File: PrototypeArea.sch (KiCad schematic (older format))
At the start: 16 parts, among them P12 CONN_20, P14 CONN_20, P15 CONN_5, P16 CONN_20, P17 CONN_20, P18 CONN_20, P19 CONN_20, P20 CONN_20, P21 CONN_20, P22 CONN_20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

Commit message: Changed the footprint of the PIC to the correct one. Changed the layout of the development area, to be more suited for development Changed the layout of the reset button and programmer header. The programmer header now needs to be a 90deg header, for the pickit3 to fit Added components for the mounting holes and OSHW logos.
Signed-off-by: Kolijn Wolfaardt <kolijn.wolfaardt2gmail.com>
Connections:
- wire segments 58 -> 70

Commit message: Changed to FTDI chip, cut space from development area
An FTDI chip was added to provide the USB communications rather than the PIC
A jumper is available to choose if the USB datalines go to the FTDI chip or the
PIC.

The development area was reduced to provide space for the FTDI chip.

Signed-off-by: Kolijn Wolfaardt <kolijn.wolfaardt@gmail.com>
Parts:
- removed P12, P14, P16, P17, P18, P19, P20, P21, P22, P5, P6, P7: CONN_20, symbol CONN_20
- added P12, P14, P16, P17, P18, P19, P20, P21, P22, P5, P6, P7: CONN_12, symbol CONN_12
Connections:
- wire segments 70 -> 40

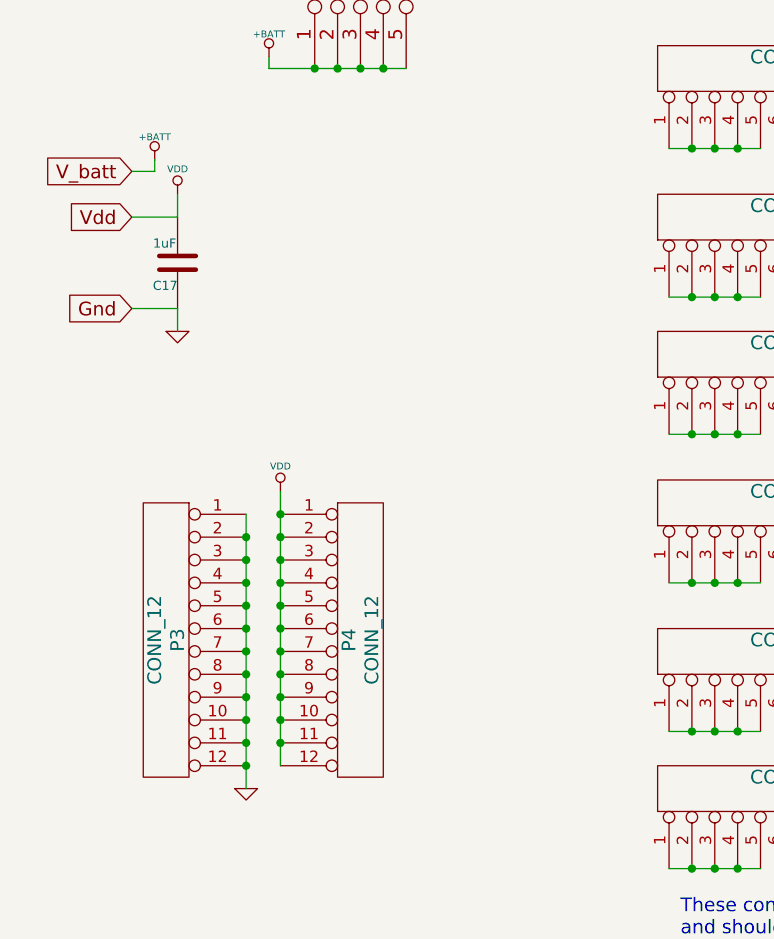
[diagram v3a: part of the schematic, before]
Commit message: Changed the board to use 3.3v rather than 5v. Total new layout.
Since the FTDI chip cannot communicate with the 5v PIC. So run
the PIC at 3.3v This limits the maximum crystal frequency of
the pic, but 4MHz is fine. the internal usb regulator is no
longer used and is replaced with the external one.

The 3.3v regulator get it's 5v from the selected 5v source.
5v is still used by the FTDI chip and the Motor driver.

Signed-off-by: Kolijn Wolfaardt <kolijn.wolfaardt@gmail.com>
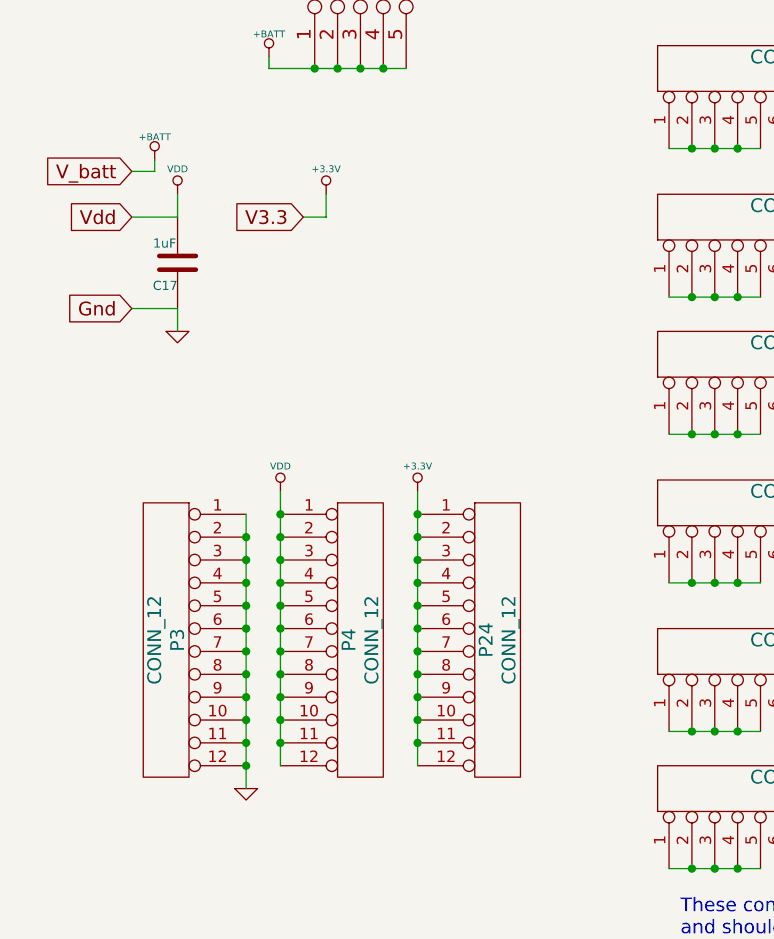
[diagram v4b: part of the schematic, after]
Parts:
- added P24: CONN_12, symbol CONN_12
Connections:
- new net +3.3V: P24.1 (P1), P24.10 (P10), P24.11 (P11), P24.12 (P12), P24.2 (P2), P24.3 (P3), P24.4 (P4), P24.5 (P5), P24.6 (P6), P24.7 (P7), P24.8 (P8), P24.9 (P9)
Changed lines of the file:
@@
 LIBS:l293
 LIBS:FT230x
+LIBS:33vReg
 LIBS:Robotics Board-cache
 EELAYER 27 0
@@
 Sheet 6 6
 Title ""
-Date "19 apr 2014"
+Date "20 apr 2014"
 Rev ""
 Comp ""
@@
 $EndDescr
 $Comp
-L +BATT #PWR054
+L +BATT #PWR061
 U 1 1 52F479E1
 P 1900 1100
-F 0 "#PWR054" H 1900 1050 20  0001 C CNN
+F 0 "#PWR061" H 1900 1050 20  0001 C CNN
 F 1 "+BATT" H 1900 1200 30  0000 C CNN
 F 2 "" H 1900 1100 60  0000 C CNN
@@
 $EndComp
 $Comp
-L GND #PWR055
+L GND #PWR062
 U 1 1 52F47A1B
 P 1800 4300
-F 0 "#PWR055" H 1800 4300 30  0001 C CNN
+F 0 "#PWR062" H 1800 4300 30  0001 C CNN
 F 1 "GND" H 1800 4230 30  0001 C CNN
 F 2 "" H 1800 4300 60  0000 C CNN
@@
 $EndComp
 $Comp
-L VDD #PWR056
+L VDD #PWR063
 U 1 1 52F47A2F
 P 1950 3000
-F 0 "#PWR056" H 1950 3100 30  0001 C CNN
+F 0 "#PWR063" H 1950 3100 30  0001 C CNN
 F 1 "VDD" H 1950 3110 30  0000 C CNN
 F 2 "" H 1950 3000 60  0000 C CNN
@@
 V_batt
 $Comp
-L +BATT #PWR057
+L +BATT #PWR064
 U 1 1 52F8A3F3
 P 1400 1550
-F 0 "#PWR057" H 1400 1500 20  0001 C CNN
+F 0 "#PWR064" H 1400 1500 20  0001 C CNN
 F 1 "+BATT" H 1400 1650 30  0000 C CNN
 F 2 "" H 1400 1550 60  0000 C CNN
@@
 $EndComp
 $Comp
-L GND #PWR058
+L GND #PWR065
 U 1 1 52F8A5C7
 P 1500 2300
-F 0 "#PWR058" H 1500 2300 30  0001 C CNN
+F 0 "#PWR065" H 1500 2300 30  0001 C CNN
 F 1 "GND" H 1500 2230 30  0001 C CNN
 F 2 "" H 1500 2300 60  0000 C CNN
@@
 $EndComp
 $Comp
-L VDD #PWR059
+L VDD #PWR066
 U 1 1 52F8A5CD
 P 1500 1700
-F 0 "#PWR059" H 1500 1800 30  0001 C CNN
+F 0 "#PWR066" H 1500 1800 30  0001 C CNN
 F 1 "VDD" H 1500 1810 30  0000 C CNN
 F 2 "" H 1500 1700 60  0000 C CNN
@@
 Connection ~ 5650 1600
 Connection ~ 6050 4650
+$Comp
+L CONN_12 P24
+U 1 1 53538B70
+P 2900 3650
+F 0 "P24" V 2850 3650 60  0000 C CNN
+F 1 "CONN_12" V 2950 3650 60  0000 C CNN
+F 2 "" H 2900 3650 60  0000 C CNN
+F 3 "" H 2900 3650 60  0000 C CNN
+	1    2900 3650
+	1    0    0    -1
+$EndComp
+Wire Wire Line
+	2550 3000 2550 4200
+Connection ~ 2550 4100
+Connection ~ 2550 4000
+Connection ~ 2550 3900
+Connection ~ 2550 3800
+Connection ~ 2550 3700
+Connection ~ 2550 3600
+Connection ~ 2550 3500
+Connection ~ 2550 3400
+Connection ~ 2550 3300
+Connection ~ 2550 3200
+Text GLabel 2050 1800 0    60   Input ~ 0
+V3.3
+$Comp
+L +3.3V #PWR067
+U 1 1 53539288
+P 2150 1700
+F 0 "#PWR067" H 2150 1660 30  0001 C CNN
+F 1 "+3.3V" H 2150 1810 30  0000 C CNN
+F 2 "" H 2150 1700 60  0000 C CNN
+F 3 "" H 2150 1700 60  0000 C CNN
+	1    2150 1700
+	1    0    0    -1
+$EndComp
+Wire Wire Line
+	2050 1800 2150 1800
+Wire Wire Line
+	2150 1800 2150 1700
+$Comp
+L +3.3V #PWR068
+U 1 1 5353933F
+P 2550 3000
+F 0 "#PWR068" H 2550 2960 30  0001 C CNN
+F 1 "+3.3V" H 2550 3110 30  0000 C CNN
+F 2 "" H 2550 3000 60  0000 C CNN
+F 3 "" H 2550 3000 60  0000 C CNN
+	1    2550 3000
+	1    0    0    -1
+$EndComp
+Connection ~ 2550 3100
 $EndSCHEMATC
